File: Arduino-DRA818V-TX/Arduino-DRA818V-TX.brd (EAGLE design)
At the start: 68.6 x 53.3 mm, 16 parts, among them M1 ARDUINO_R3_ICSP

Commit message: Adding Arduino-DRA818V-TX Board
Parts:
- removed JP9: (no value), carduino:1X06-BIG
- removed U$1: PINHD-1X10, adafruit:1X10-BIG
- removed U$36: (no value), microbuilder:ADAFRUIT_9MM
- removed U$4, U$7: PERFHOLE, Atmex:PERFHOLE
- added C3, C9: 1u, resistor:C1206
- added C4, C5, C6, C7, C8: 100n, resistor:C1206
- added JP2: (no value), carduino:1X06-BIG
- added JP3: (no value), adafruit:1X10-BIG
- added R3: 560, resistor:R1206
- added R4: 10k, pot:CA6V
- added T1: (no value), transistor:TO92-CBE
- added X1: SMA, con-coax:LTI-SASF54GT
- added X2: SMA, con-coax:J502-ND-142-0701-801/806
- C1: value (none) -> 1n; device rcl-ez:C025-025X050 -> resistor:C1206
- C2: value (none) -> 10n; device rcl-ez:C025-025X050 -> resistor:C1206
- R1: value (none) -> 560; device rcl-ez:0207/5V -> resistor:R1206
- R2: value (none) -> 1k; device rcl-ez:0207/5V -> resistor:R1206
- moved C2 150.0 mm to (-52.1, 99.1), turned to 0 degrees
- moved JP4 139.3 mm to (-72.4, 104.1), turned to 0 degrees
- moved JP1 131.3 mm to (-50.8, 104.1), turned to 0 degrees
- moved R2 126.7 mm to (-72.4, 99.1), turned to 0 degrees
- moved LED2 123.9 mm to (-47.0, 110.5), turned to 0 degrees
- moved C1 123.8 mm to (-47.0, 99.1)
- moved RESET 100.5 mm to (-77.5, 61.0), turned to 0 degrees
- moved R1 90.4 mm to (-67.3, 99.1)
- moved M1 81.3 mm to (-81.3, 1.27)
- moved LED1 72.2 mm to (-36.8, 110.5), turned to 0 degrees
- moved U$2 45.1 mm to (-25.4, 74.9), turned to 0 degrees
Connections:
- net 3.3V renamed N$17
- removed net N$135: JP4.6, M1.D5
- removed net N$145: JP4.7, M1.D6
- removed net N$152: JP4.8, M1.D7
- removed net N$154: M1.SCL, U$1.1
- removed net N$16: R1.2, U$7.1
- removed net N$164: M1.SDA, U$1.2
- removed net N$40: R2.2, U$4.1
- removed net N$45: M1.D12, U$1.6
- removed net N$54: M1.D11, U$1.7
- removed net N$55: M1.D10, U$1.8
- removed net N$56: M1.D9, U$1.9
- removed net N$57: M1.D8, U$1.10
- removed net N$58: JP9.1, M1.A0
- removed net N$59: JP9.2, M1.A1
- removed net N$70: JP9.3, M1.A2
- removed net N$88: JP9.4, M1.A3
- removed net N$89: JP9.5, M1.A4
- removed net N$92: JP9.6, M1.A5
- new net AF_NORM: C9.2, U$2.18
- new net AF_OUT: JP3.6, M1.D12, R4.A
- new net LED_BUILTIN: JP3.5, M1.D13, R3.2
- new net N$1: JP3.1, M1.SCL
- new net N$21: JP2.1, M1.A0
- new net N$22: JP2.2, M1.A1
- new net N$23: JP2.3, M1.A2
- new net N$24: JP2.4, M1.A3
- new net N$25: JP2.5, M1.A4
- new net N$26: JP2.6, M1.A5
- new net N$3: JP3.3, M1.AREF
- new net N$7: C6.1, R2.1, T1.B
- new net N$9: C8.1, C9.1, R4.S
- new net PD: C4.1, JP4.7, M1.D6, U$2.6
- new net POW: C5.1, JP4.6, M1.D5, U$2.7
- new net PTT: JP4.8, M1.D7, R2.2
- new net PTT_SW: C7.1, T1.C, U$2.5
- new net RXD_DRJ: JP3.8, M1.D10
- new net RXD_GPS: JP3.10, M1.D8, U$2.16
- new net TXD_DRJ: JP3.7, M1.D11
- new net TXD_GPS: JP3.9, M1.D9, U$2.17
- net +5V: now also C3.1, R1.2, U$2.8
- net GND: now also C3.2, C4.2, C5.2, C6.2, C7.2, C8.2, JP3.4, R4.E, T1.E, U$2.10, U$2.9, X1.2, X1.3, X1.4, X1.5, X2.G@1, X2.G@2, X2.G@3, X2.G@4; no longer U$1.4
- net N$2: now also JP3.2, M1.SDA; no longer M1.AREF, U$1.3
- net N$41: now also R1.1; no longer R2.1
- net N$5: now also U$2.12, X1.1, X2.1; no longer M1.D13, U$1.5
- net N$8: now also R3.1; no longer R1.1
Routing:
- net GND: track 95.7 -> 0.00 mm
- net RESET: track 37.3 -> 0.00 mm
- net +5V: track 34.0 -> 0.00 mm
- net N$41: track 4.46 -> 0.00 mm
- net N$8: track 4.29 -> 0.00 mm
- net N$92: track 3.81 -> 0.00 mm
- net N$89: track 3.81 -> 0.00 mm
- net N$88: track 3.81 -> 0.00 mm
- net N$70: track 3.81 -> 0.00 mm
- net N$59: track 3.81 -> 0.00 mm
- net N$58: track 3.81 -> 0.00 mm
- net N$4: track 3.81 -> 0.00 mm
- net N$20: track 3.81 -> 0.00 mm
- net N$19: track 3.81 -> 0.00 mm
- net N$17: track 3.81 -> 0.00 mm
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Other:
- board size 68.6 x 53.3 mm -> 160 x 100 mm
- board text removed: "+"
- board text removed: "5V"
- board text removed: "Analog In"
- board text removed: "Digital I/O"
- board text removed: "GND"
- board text removed: "ICSP"
- board text removed: "ProtoShield v6"
- board text removed: "Reset"
- board text removed: "http://www.ladyada.net/make/pshield"

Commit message: Removing Female header
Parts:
- removed JP1, JP4: (no value), carduino:1X08-BIG
- removed JP2: (no value), carduino:1X06-BIG
- removed JP3: (no value), adafruit:1X10-BIG
- T1: device transistor:TO92-CBE -> transistor:SOT23-BEC
- moved T1 144.7 mm to (57.5, 72.7), turned to 180 degrees
- moved C3 137.7 mm to (78.1, 73.3), turned to 90 degrees
- moved R2 132.9 mm to (58.7, 77.5), turned to 90 degrees
- moved C2 130.2 mm to (75.6, 73.3), turned to 90 degrees
- moved X2 128.6 mm to (83.2, 48.9), turned to 180 degrees
- moved X1 128.4 mm to (68.6, 41.9)
- moved R1 123.2 mm to (40.3, 39.1)
- moved R3 122.9 mm to (43.5, 77.5), turned to 90 degrees
- moved C1 122.7 mm to (73.0, 73.3), turned to 90 degrees
- moved C9 115.6 mm to (40.3, 45.7)
- moved LED2 106.8 mm to (32.7, 39.4)
- moved RESET 101.8 mm to (21.3, 36.2), turned to 180 degrees
- moved R4 100.8 mm to (32.7, 48.3), turned to 180 degrees
- moved M1 100.6 mm to (14.6, 31.8)
- moved C7 100.2 mm to (61.3, 73.3), turned to 90 degrees
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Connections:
- removed net N$1: JP3.1, M1.SCL
- removed net N$17: JP1.5, M1.3V
- removed net N$19: JP1.7, M1.IOREF
- removed net N$2: JP3.2, M1.SDA
- removed net N$20: JP1.8, M1.RESERVED
- removed net N$21: JP2.1, M1.A0
- removed net N$22: JP2.2, M1.A1
- removed net N$23: JP2.3, M1.A2
- removed net N$24: JP2.4, M1.A3
- removed net N$25: JP2.5, M1.A4
- removed net N$26: JP2.6, M1.A5
- removed net N$27: JP4.1, M1.D0
- removed net N$28: JP4.2, M1.D1
- removed net N$29: JP4.3, M1.D2
- removed net N$3: JP3.3, M1.AREF
- removed net N$30: JP4.4, M1.D3
- removed net N$31: JP4.5, M1.D4
- removed net N$4: JP1.1, M1.VIN
- new net 3V: M1.3V
- new net VIN: M1.VIN
- net +5V: no longer JP1.4
- net AF_OUT: no longer JP3.6
- net GND: no longer JP1.2, JP1.3, JP3.4
- net LED_BUILTIN: no longer JP3.5
- net PD: no longer JP4.7
- net POW: no longer JP4.6
- net PTT: no longer JP4.8
- net RESET: no longer JP1.6
- net RXD_DRJ: no longer JP3.8
- net RXD_GPS: no longer JP3.10
- net TXD_DRJ: no longer JP3.7
- net TXD_GPS: no longer JP3.9
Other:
- board size 160 x 100 mm -> 68.6 x 53.3 mm

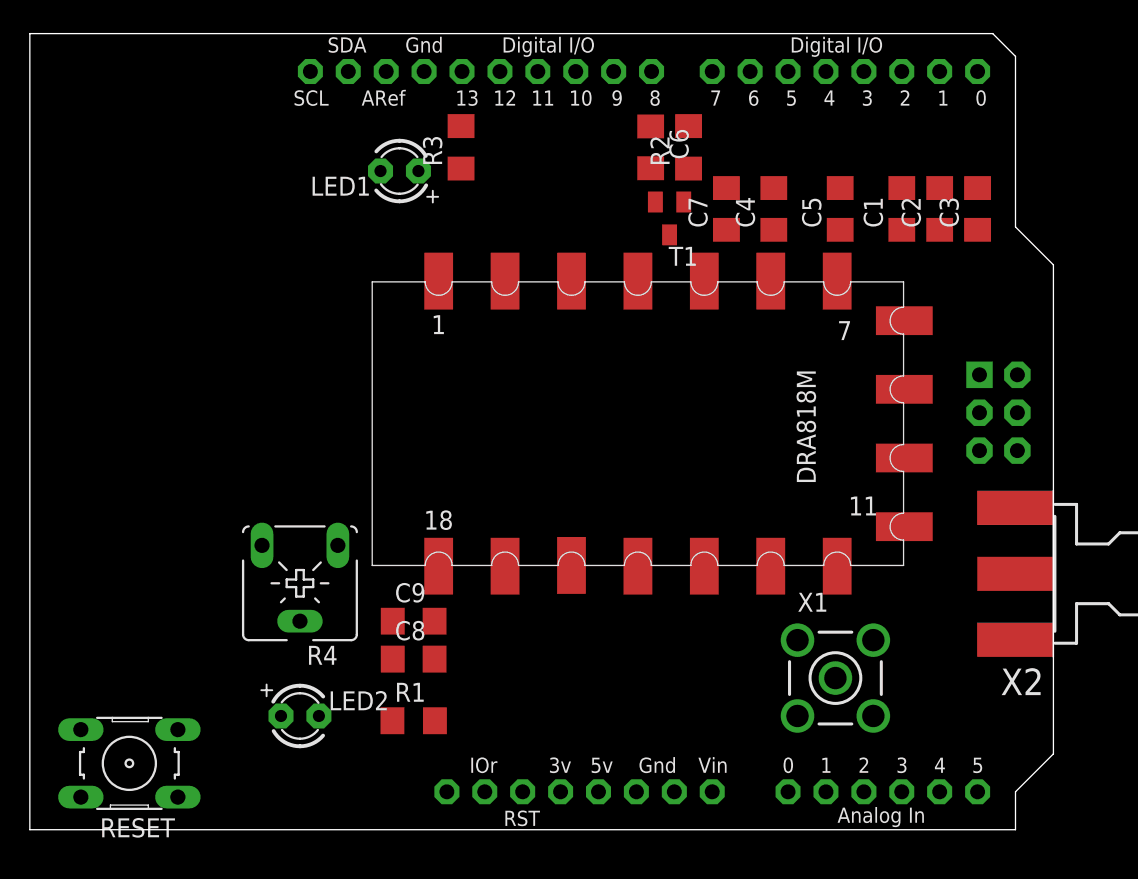
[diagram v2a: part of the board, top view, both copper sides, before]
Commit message: Apply SparkFun DRU
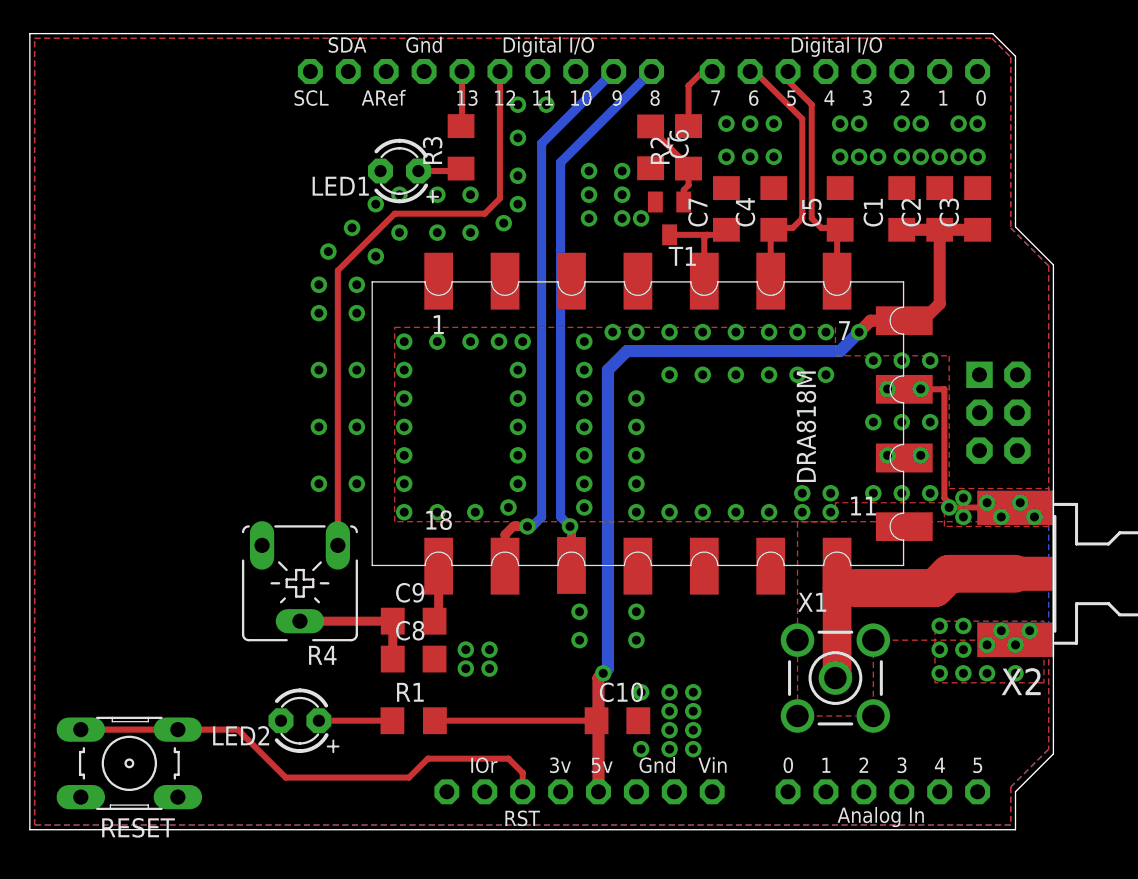
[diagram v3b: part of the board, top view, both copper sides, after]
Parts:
- added C10: 1n, resistor:C1206
- moved LED2 0.32 mm to (32.7, 39.1), turned to 180 degrees
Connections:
- net +5V: now also C10.1
- net GND: now also C10.2
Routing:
- net +5V: track 0.00 -> 73.6 mm, vias 0 -> 2
- net AF_OUT: track 0.00 -> 39.8 mm
- net TXD_GPS: track 0.00 -> 36.9 mm, vias 0 -> 1
- net RXD_GPS: track 0.00 -> 35.9 mm, vias 0 -> 1
- net RESET: track 0.00 -> 33.1 mm
- net N$5: track 0.00 -> 19.9 mm
- net PD: track 0.00 -> 17.2 mm
- net GND: track 0.00 -> 16.8 mm, vias 0 -> 156
- net POW: track 0.00 -> 16.2 mm
- net N$9: track 0.00 -> 8.76 mm
- net PTT_SW: track 0.00 -> 7.14 mm
- net N$7: track 0.00 -> 6.25 mm
- net N$41: track 0.00 -> 4.93 mm
- net PTT: track 0.00 -> 4.69 mm
- net AF_NORM: track 0.00 -> 3.80 mm
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- added copper zone on layer 1, net GND
- added copper zone on layer 16, net GND

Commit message: Apply Polygon Pour
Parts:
- renumbered U$2 to DRA818V
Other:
- board text added: "ARDUINO TX-818V SHIELD - v1.0"
- board text added: "HANDIKO - YD1SDL"
- board text added: "www.github.com/handiko"
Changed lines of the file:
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@@
 <layer number="27" name="tValues" color="7" fill="1" visible="yes" active="yes"/>
 <layer number="28" name="bValues" color="7" fill="1" visible="yes" active="yes"/>
-<layer number="29" name="tStop" color="7" fill="3" visible="no" active="yes"/>
-<layer number="30" name="bStop" color="7" fill="6" visible="no" active="yes"/>
+<layer number="29" name="tStop" color="7" fill="3" visible="yes" active="yes"/>
+<layer number="30" name="bStop" color="7" fill="6" visible="yes" active="yes"/>
 <layer number="31" name="tCream" color="7" fill="4" visible="no" active="yes"/>
 <layer number="32" name="bCream" color="7" fill="5" visible="no" active="yes"/>
@@
 <board>
 <plain>
+<text x="20.32" y="43.4975" size="1.778" layer="29" ratio="10" rot="R90">ARDUINO TX-818V SHIELD - v1.0</text>
+<text x="23.495" y="43.4975" size="1.6764" layer="29" ratio="10" rot="R90">HANDIKO - YD1SDL</text>
+<text x="26.3525" y="43.4975" size="1.6764" layer="29" ratio="10" rot="R90">www.github.com/handiko</text>
 </plain>
 <attributes>
@@
 <attribute name="MPN" value="B3F-1000" x="21.2725" y="36.195" size="1.778" layer="27" rot="R180" display="off"/>
 </element>
-<element name="U$2" library="dorji" package="DRA818A" value="" x="55.245" y="59.055" rot="R270"/>
+<element name="DRA818V" library="dorji" package="DRA818A" value="" x="55.245" y="59.055" smashed="yes" rot="R270">
+<attribute name="NAME" x="57.5075" y="58.8725" size="1.27" layer="49"/>
+</element>
 <element name="X1" library="con-coax" package="LTI-SASF54GT" value="SMA" x="68.58" y="41.91">
 <attribute name="MF" value="" x="68.58" y="41.91" size="1.778" layer="27" display="off"/>
@@
 <signal name="+5V">
 <contactref element="M1" pad="5V"/>
-<contactref element="U$2" pad="8"/>
+<contactref element="DRA818V" pad="8"/>
 <contactref element="C3" pad="1"/>
 <contactref element="C1" pad="1"/>
@@
 <contactref element="M1" pad="GND"/>
 <contactref element="M1" pad="GND@3"/>
-<contactref element="U$2" pad="9"/>
-<contactref element="U$2" pad="10"/>
+<contactref element="DRA818V" pad="9"/>
+<contactref element="DRA818V" pad="10"/>
 <contactref element="C1" pad="2"/>
 <contactref element="C2" pad="2"/>
@@
 <signal name="TXD_GPS">
 <contactref element="M1" pad="D9"/>
-<contactref element="U$2" pad="17"/>
+<contactref element="DRA818V" pad="17"/>
 <wire x1="46.445" y1="49.405" x2="46.445" y2="51.525" width="0.6096" layer="1"/>
 <wire x1="46.445" y1="51.525" x2="46.99" y2="52.07" width="0.6096" layer="1"/>
@@
 <signal name="RXD_GPS">
 <contactref element="M1" pad="D8"/>
-<contactref element="U$2" pad="16"/>
+<contactref element="DRA818V" pad="16"/>
 <wire x1="50.895" y1="49.455" x2="50.895" y2="51.975" width="0.6096" layer="1"/>
 <wire x1="50.895" y1="51.975" x2="50.8" y2="52.07" width="0.6096" layer="1"/>
@@
 <signal name="POW">
 <contactref element="M1" pad="D5"/>
-<contactref element="U$2" pad="7"/>
+<contactref element="DRA818V" pad="7"/>
 <contactref element="C5" pad="1"/>
 <wire x1="65.405" y1="82.55" x2="65.405" y2="81.915" width="0.4064" layer="1"/>
@@
 <signal name="PD">
 <contactref element="M1" pad="D6"/>
-<contactref element="U$2" pad="6"/>
+<contactref element="DRA818V" pad="6"/>
 <contactref element="C4" pad="1"/>
 <wire x1="62.865" y1="82.55" x2="63.1825" y2="82.55" width="0.4064" layer="1"/>
@@
 </signal>
 <signal name="PTT_SW">
-<contactref element="U$2" pad="5"/>
+<contactref element="DRA818V" pad="5"/>
 <contactref element="C7" pad="1"/>
 <contactref element="T1" pad="C"/>
@@
 </signal>
 <signal name="AF_NORM">
-<contactref element="U$2" pad="18"/>
+<contactref element="DRA818V" pad="18"/>
 <contactref element="C9" pad="2"/>
 <wire x1="41.995" y1="49.405" x2="41.995" y2="45.9925" width="0.6096" layer="1"/>
@@
 </signal>
 <signal name="N$5">
-<contactref element="U$2" pad="12"/>
+<contactref element="DRA818V" pad="12"/>
 <contactref element="X1" pad="1"/>
 <contactref element="X2" pad="1"/>

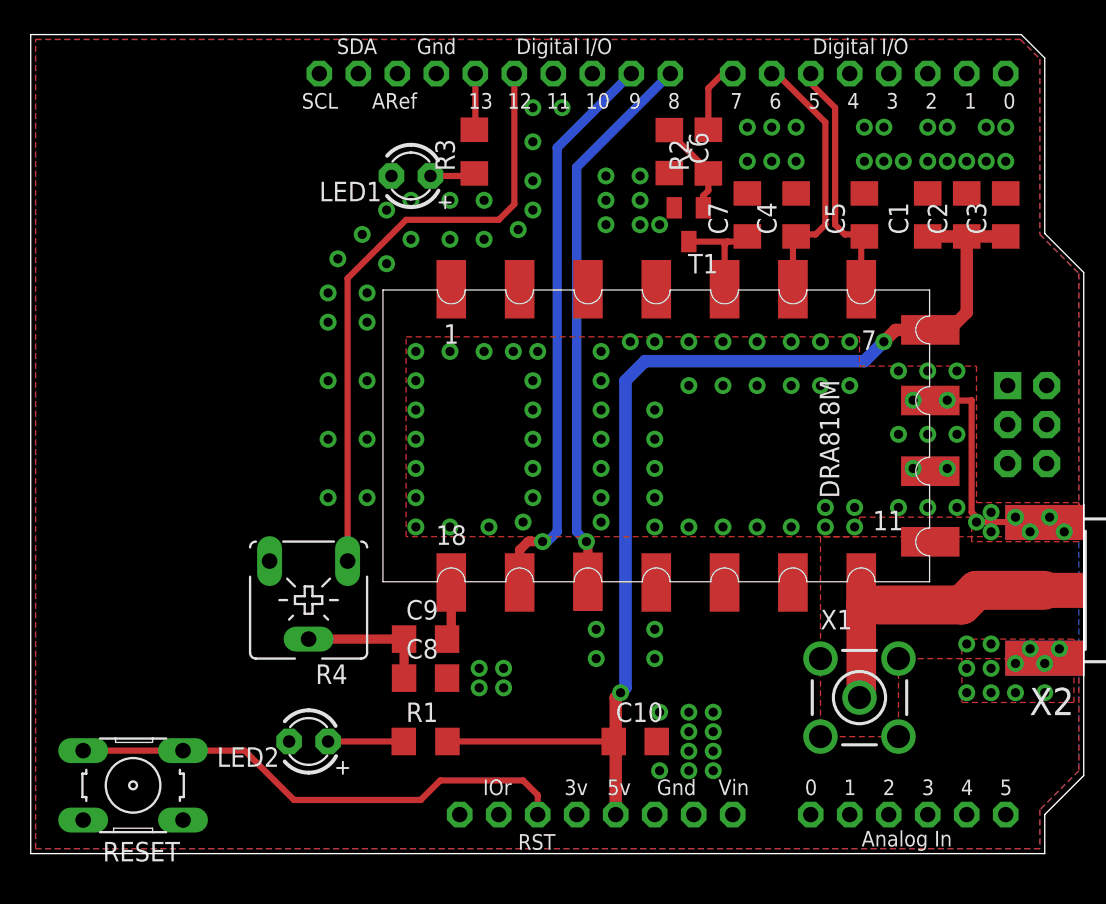
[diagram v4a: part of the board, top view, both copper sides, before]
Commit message: Adding GPS Port
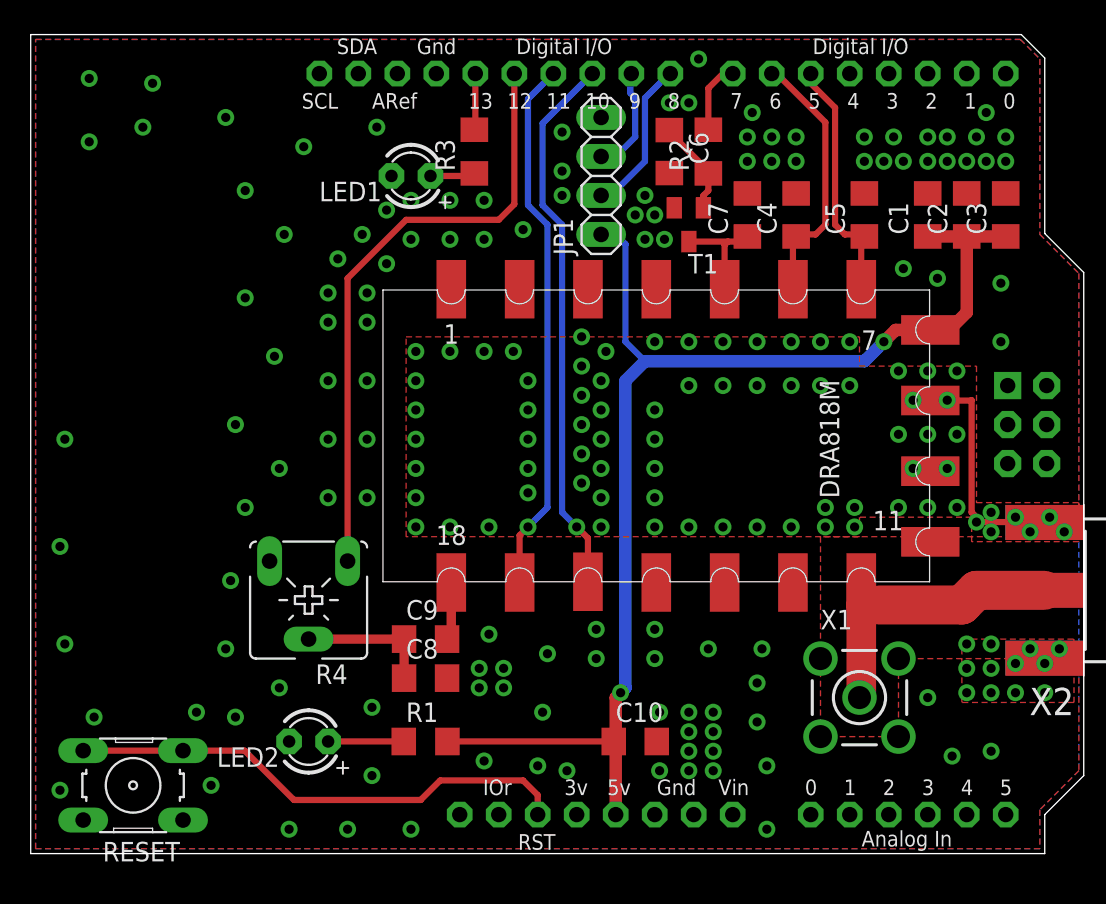
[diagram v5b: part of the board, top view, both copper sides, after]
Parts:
- added JP1: (no value), pinhead:1X04
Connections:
- net +5V: now also JP1.1
- net GND: now also JP1.4
- net RXD_DRJ: now also DRA818V.16
- net RXD_GPS: now also JP1.2; no longer DRA818V.16
- net TXD_DRJ: now also DRA818V.17
- net TXD_GPS: now also JP1.3; no longer DRA818V.17
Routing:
- net RXD_DRJ: track 0.00 -> 35.7 mm, vias 0 -> 1
- net TXD_DRJ: track 0.00 -> 35.1 mm, vias 0 -> 1
- net TXD_GPS: track 36.9 -> 7.03 mm, vias 1 -> 0
- net RXD_GPS: track 35.9 -> 10.2 mm, vias 1 -> 0
- net +5V: track 73.6 -> 83.6 mm
- net GND: vias 156 -> 209
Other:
- board text added: "ARDUINO TX-818V SHIELD"
- board text removed: "ARDUINO TX-818V SHIELD - v1.0"

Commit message: Adding GPS Port
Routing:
- net GND: track 16.8 -> 18.6 mm
